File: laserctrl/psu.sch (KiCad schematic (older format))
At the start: 39 parts, among them U1 MC34063

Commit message: Added a todo list so I don't forget the last bits and tried annotating different ways
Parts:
- gave numbers to parts that had none: 19
- renumbered C5 to C72, C6 to C73, C7 to C74, C8 to C75, C10 to C76, C4 to C80, D1 to D41, R5 to R86, R7 to R87, R6 to R88, U1 to U8

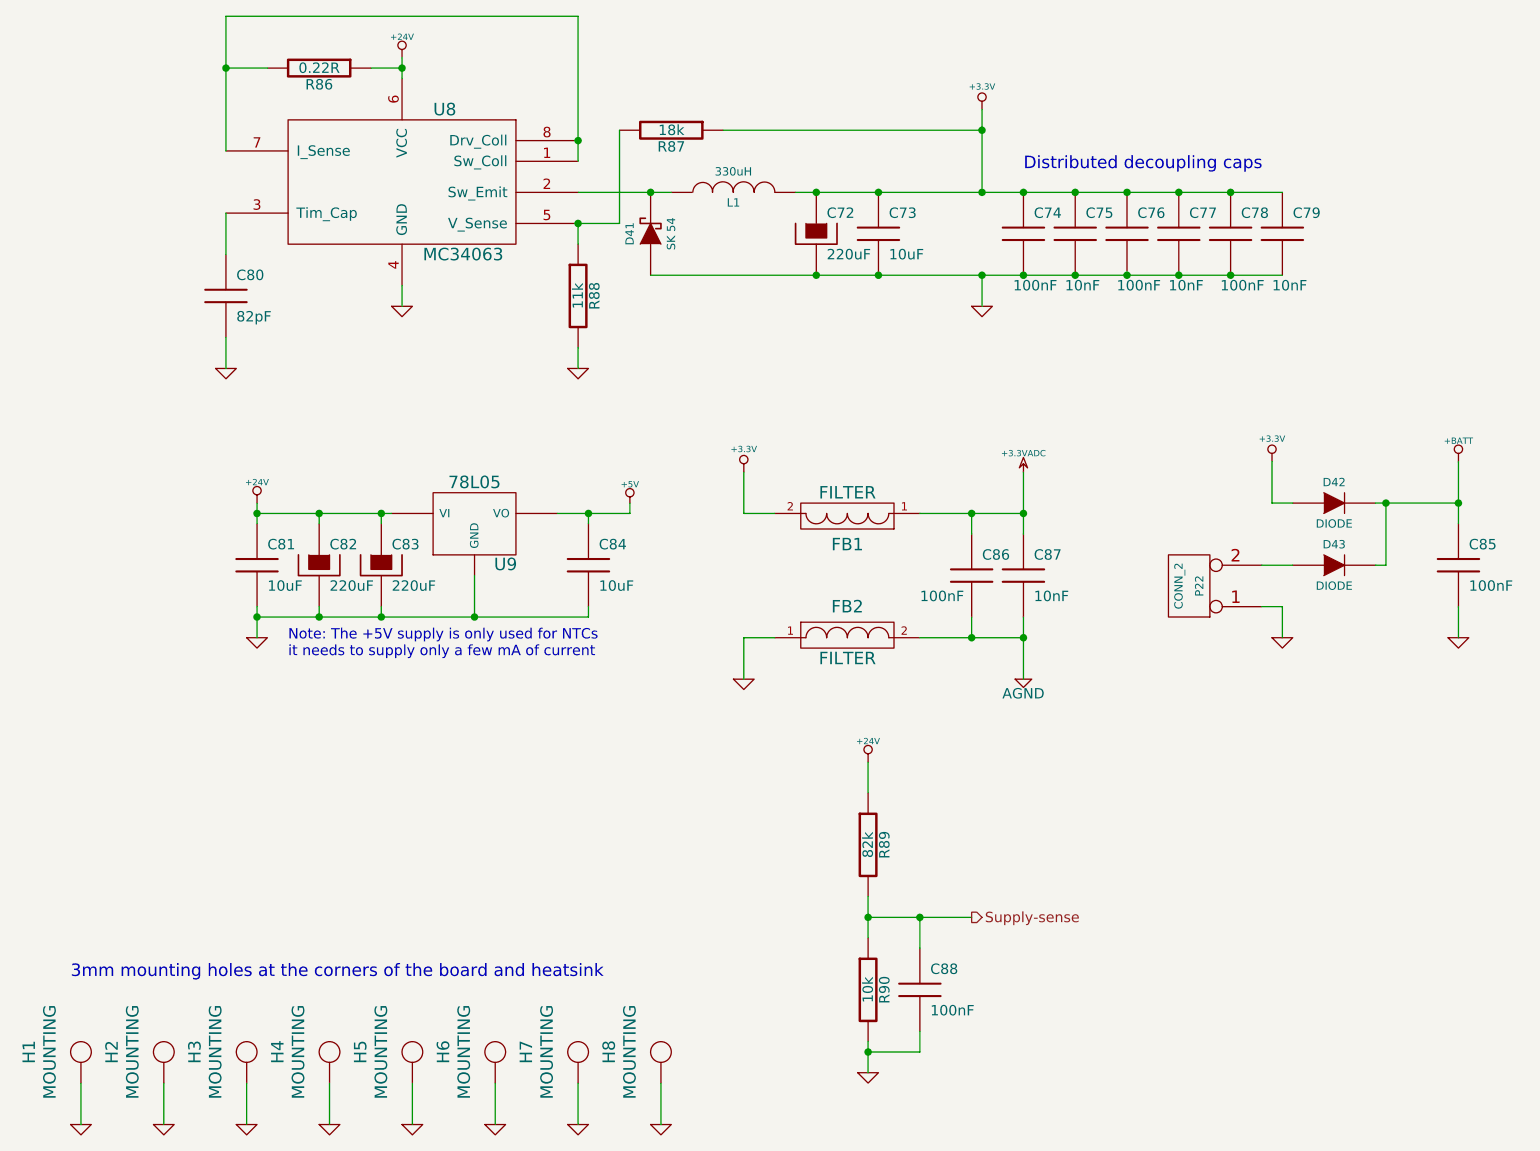
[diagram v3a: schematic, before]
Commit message: Started assigning footprints
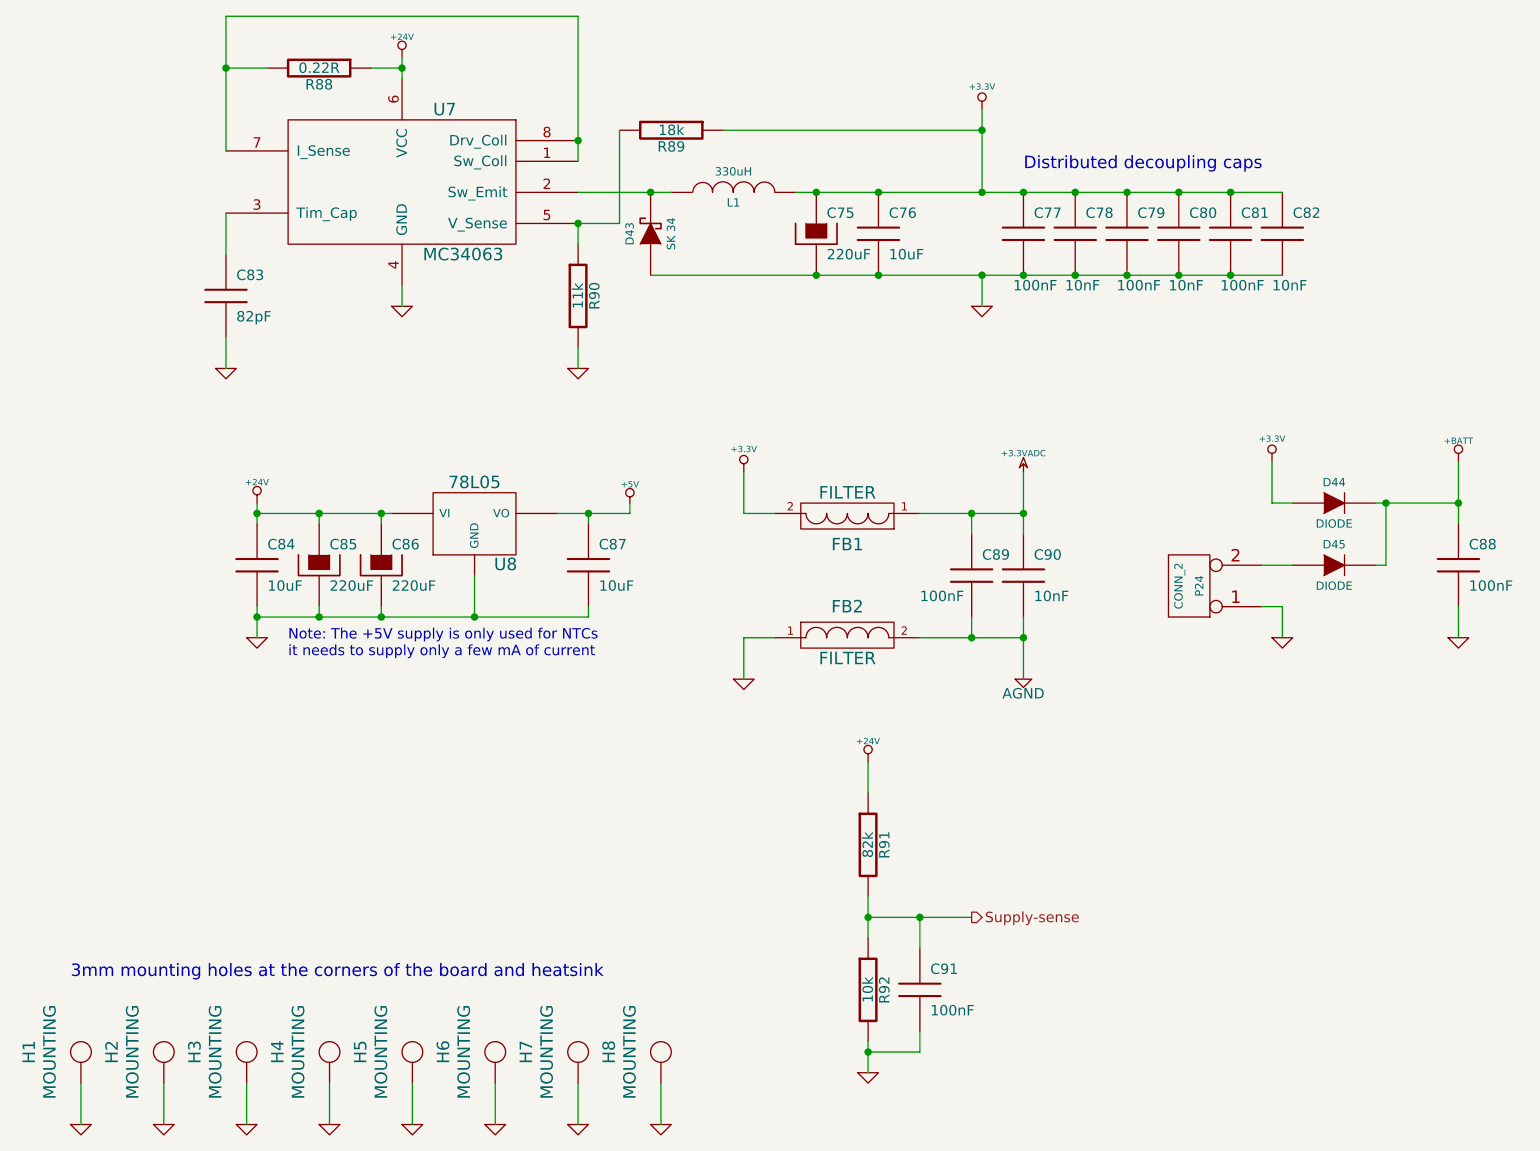
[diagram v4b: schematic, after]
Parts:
- D43: renamed from D41; value SK 54 -> SK 34
- renumbered C72 to C75, C73 to C76, C74 to C77, C75 to C78, C76 to C79, C77 to C80, C78 to C81, C79 to C82, C80 to C83, C81 to C84, C82 to C85, C83 to C86, C84 to C87, C85 to C88, C86 to C89, C87 to C90, C88 to C91, D42 to D44, D43 to D45, P22 to P24, R86 to R88, R87 to R89, R88 to R90, R89 to R91, R90 to R92, U8 to U7, U9 to U8

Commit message: Started some cleaning up
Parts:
- removed C78, C80, C82, C90: 10nF, symbol C
- C75: value 220uF -> 1mF/10V
- C76: value 10uF -> 22uF/6.3V
- C84: value 10uF -> 10uF/35V
- C85, C86: value 220uF -> 1.5mF/35V
- C87: value 10uF -> 22uF/6.3
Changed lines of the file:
@@
-EESchema Schematic File Version 2  date 2011-11-08T22:27:11 CET
+EESchema Schematic File Version 2  date 2011-11-09T19:37:00 CET
 LIBS:power
 LIBS:device
@@
 LIBS:atmel
 LIBS:microsd
-LIBS:laserctrl-cache
+LIBS:jumper3
 EELAYER 25  0
 EELAYER END
 $Descr A4 11700 8267
 encoding utf-8
-Sheet 12 12
+Sheet 10 10
 Title ""
-Date "8 nov 2011"
+Date "9 nov 2011"
 Rev ""
 Comp ""
@@
 Comment4 ""
 $EndDescr
-Text HLabel 5800 6100 2    50   Output ~ 0
-Supply-sense
+Wire Wire Line
+	7050 3000 4250 3000
+Wire Wire Line
+	6050 4950 6050 4750
 Connection ~ 5550 6100
 Wire Wire Line
@@
 Connection ~ 5800 4150
 Wire Wire Line
-	6050 4150 5550 4150
+	5550 4150 6050 4150
 Wire Wire Line
 	4850 4150 4700 4150
 Wire Wire Line
 	4700 4150 4700 3950
-Connection ~ 6800 3000
 Connection ~ 6550 2600
-Connection ~ 6800 2600
-Wire Wire Line
-	4950 2600 7300 2600
 Wire Wire Line
 	3500 7100 3500 6900
@@
 Connection ~ 5050 3000
 Connection ~ 5350 3000
-Connection ~ 6300 3000
-Connection ~ 6300 2600
 Connection ~ 5850 2600
 Wire Wire Line
@@
 Wire Wire Line
 	5850 2200 5850 2600
-Connection ~ 7050 2600
 Connection ~ 6550 3000
 Wire Wire Line
-	7300 3000 4250 3000
-Connection ~ 7050 3000
-Wire Wire Line
 	5800 4150 5800 4250
-Wire Wire Line
-	6050 3950 6050 4250
-Connection ~ 6050 4150
 Wire Wire Line
 	7750 4100 8150 4100
@@
 	7300 4600 7200 4600
 Wire Wire Line
-	6050 4950 6050 4650
-Connection ~ 6050 4750
-Wire Wire Line
 	2350 4650 3950 4650
 Wire Wire Line
@@
 	5550 6750 5300 6750
 Connection ~ 5300 6750
+Wire Wire Line
+	6050 4150 6050 3950
+Wire Wire Line
+	7050 2600 4950 2600
+Text HLabel 5800 6100 2    50   Output ~ 0
+Supply-sense
 $Comp
 L C C91
@@
 	1    0    0    -1
 $EndComp
-Text Notes 2500 4850 0    50   ~ 0
+Text Notes 2400 3850 0    50   ~ 0
 Note: The +5V supply is only used for NTCs\nit needs to supply only a few mA of current
 $Comp
@@
 P 2950 4400
 F 0 "C86" H 3000 4500 50  0000 L CNN
-F 1 "220uF" H 3000 4300 50  0000 L CNN
+F 1 "1.5mF/35V" H 2800 3950 50  0000 L CNN
 	1    2950 4400
 	1    0    0    -1
@@
 P 2650 4400
 F 0 "C85" H 2700 4500 50  0000 L CNN
-F 1 "220uF" H 2700 4300 50  0000 L CNN
+F 1 "1.5mF/35V" H 2500 4050 50  0000 L CNN
 	1    2650 4400
 	1    0    0    -1
@@
 P 3950 4400
 F 0 "C87" H 4000 4500 50  0000 L CNN
-F 1 "10uF" H 4000 4300 50  0000 L CNN
+F 1 "22uF/6.3" H 4000 4300 50  0000 L CNN
 	1    3950 4400
 	1    0    0    -1
@@
 P 2350 4400
 F 0 "C84" H 2400 4500 50  0000 L CNN
-F 1 "10uF" H 2400 4300 50  0000 L CNN
+F 1 "10uF/35V" H 1950 4300 50  0000 L CNN
 	1    2350 4400
 	1    0    0    -1
@@
 $EndComp
 $Comp
-L C C90
-U 1 1 4EA3E94B
-P 6050 4450
-F 0 "C90" H 6100 4550 50  0000 L CNN
-F 1 "10nF" H 6100 4350 50  0000 L CNN
-	1    6050 4450
-	1    0    0    -1
-$EndComp
-$Comp
-L C C82
-U 1 1 4EA3E691
-P 7300 2800
-F 0 "C82" H 7350 2900 50  0000 L CNN
-F 1 "10nF" H 7250 2550 50  0000 L CNN
-	1    7300 2800
-	1    0    0    -1
-$EndComp
-$Comp
 L C C81
 U 1 1 4EA3E68B
@@
 $EndComp
 $Comp
-L C C80
-U 1 1 4EA3E686
-P 6800 2800
-F 0 "C80" H 6850 2900 50  0000 L CNN
-F 1 "10nF" H 6750 2550 50  0000 L CNN
-	1    6800 2800
-	1    0    0    -1
-$EndComp
-$Comp
 L +3.3V #PWR127
 U 1 1 4EA3E60A
@@
 $EndComp
 $Comp
-L C C78
-U 1 1 4D04D38C
-P 6300 2800
-F 0 "C78" H 6350 2900 50  0000 L CNN
-F 1 "10nF" H 6250 2550 50  0000 L CNN
-	1    6300 2800
-	1    0    0    -1
-$EndComp
-$Comp
 L C C77
 U 1 1 4D04D33D
@@
 P 5350 2800
 F 0 "C76" H 5400 2900 50  0000 L CNN
-F 1 "10uF" H 5400 2700 50  0000 L CNN
+F 1 "22uF/6.3V" H 5400 2700 50  0000 L CNN
 	1    5350 2800
 	1    0    0    -1
@@
 P 5050 2800
 F 0 "C75" H 5100 2900 50  0000 L CNN
-F 1 "220uF" H 5100 2700 50  0000 L CNN
+F 1 "1mF/10V" H 4900 2500 50  0000 L CNN
 	1    5050 2800
 	1    0    0    -1
